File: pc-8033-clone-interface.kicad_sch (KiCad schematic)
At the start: 15 parts, among them J2 80s31, U2 74LS32, U3 74LS04, U4 82C55A, U5 74LS30

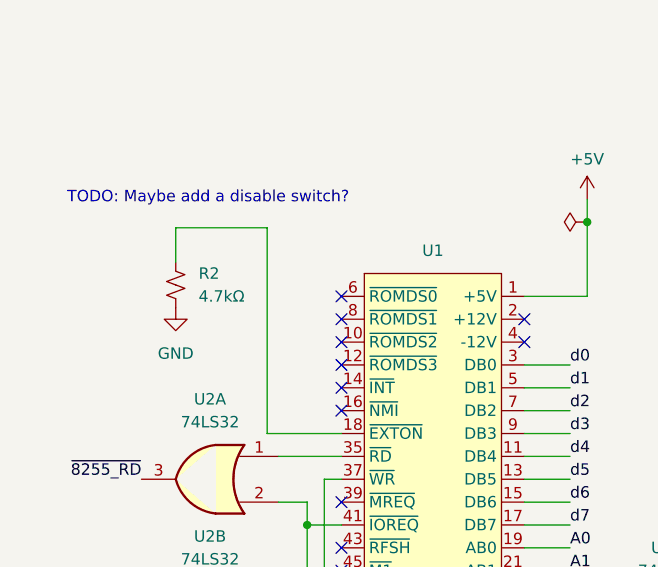
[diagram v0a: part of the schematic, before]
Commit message: Short the EXTON pin instead of trying to gently pull it down
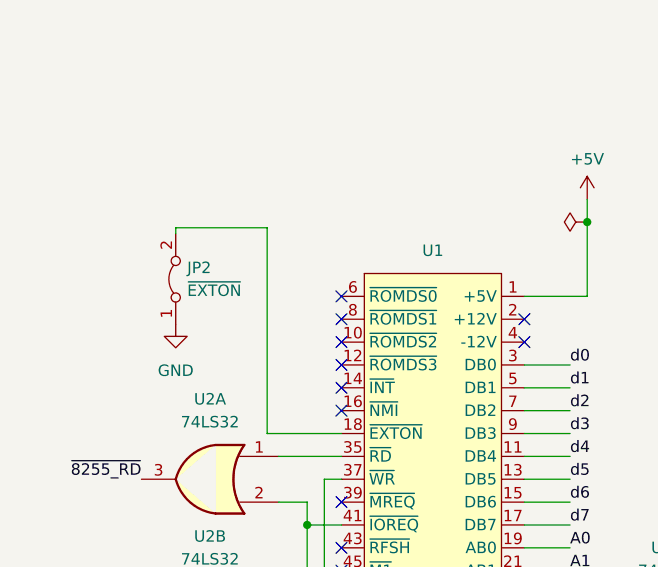
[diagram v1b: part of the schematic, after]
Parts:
- removed R2: 4.7kΩ, Resistor_THT:R_Axial_DIN0309_L9.0mm_D3.2mm_P12.70mm_Horizontal, symbol Device:R_Small_US
- added JP2: ~{EXTON}, Jumper:SolderJumper-2_P1.3mm_Bridged2Bar_Pad1.0x1.5mm, symbol Jumper:Jumper_2_Bridged
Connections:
- net GND: now also JP2.1 (A)
- net at U1.18 (~{EXTON}): now also JP2.2 (B)
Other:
- note removed: "TODO: Maybe add a disable switch?"
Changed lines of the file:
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@@
     (stroke (width 0) (type default))
   )
-  (wire (pts (xy 27.94 58.42) (xy 27.94 62.23))
+  (wire (pts (xy 27.94 58.42) (xy 27.94 59.055))
     (stroke (width 0) (type default))
   )
@@
   (text "This second inversion of reset appears to be important for timing purposes,\nas per https://blog.goo.ne.jp/tk-80/e/6ac4226f93ae2f80224ee7fcf31cb796"
     (at 166.37 158.75 0)
-    (effects (font (size 1.27 1.27)) (justify left bottom))
-  )
-  (text "TODO: Maybe add a disable switch?" (at 15.875 55.88 0)
     (effects (font (size 1.27 1.27)) (justify left bottom))
   )
@@
         (path "/9d504855-0dbe-4626-9ba5-7c5a4a75c091"
           (reference "#FLG02") (unit 1)
-        )
-      )
-    )
-  )
-  (symbol (lib_id "Device:R_Small_US") (at 27.94 64.77 0) (unit 1)
-    (in_bom yes) (on_board yes) (dnp no) (fields_autoplaced)
-    (property "Reference" "R2" (at 30.48 63.5 0)
-      (effects (font (size 1.27 1.27)) (justify left))
-    )
-    (property "Value" "4.7kΩ" (at 30.48 66.04 0)
-      (effects (font (size 1.27 1.27)) (justify left))
-    )
-    (property "Footprint" "Resistor_THT:R_Axial_DIN0309_L9.0mm_D3.2mm_P12.70mm_Horizontal" (at 27.94 64.77 0)
-      (effects (font (size 1.27 1.27)) hide)
-    )
-    (property "Datasheet" "~" (at 27.94 64.77 0)
-      (effects (font (size 1.27 1.27)) hide)
-    )
-    (pin "1")
-    (pin "2")
-    (instances
-      (project "pc-8033-clone-interface"
-        (path "/9d504855-0dbe-4626-9ba5-7c5a4a75c091"
-          (reference "R2") (unit 1)
         )
       )
@@
     )
   )
-  (symbol (lib_id "power:GND") (at 27.94 67.31 0) (unit 1)
-    (in_bom yes) (on_board yes) (dnp no) (fields_autoplaced)
-    (property "Reference" "#PWR016" (at 27.94 73.66 0)
-      (effects (font (size 1.27 1.27)) hide)
-    )
-    (property "Value" "GND" (at 27.94 72.39 0)
-      (effects (font (size 1.27 1.27)))
-    )
-    (property "Footprint" "" (at 27.94 67.31 0)
-      (effects (font (size 1.27 1.27)) hide)
-    )
-    (property "Datasheet" "" (at 27.94 67.31 0)
+  (symbol (lib_id "power:GND") (at 27.94 69.215 0) (unit 1)
+    (in_bom yes) (on_board yes) (dnp no) (fields_autoplaced)
+    (property "Reference" "#PWR016" (at 27.94 75.565 0)
+      (effects (font (size 1.27 1.27)) hide)
+    )
+    (property "Value" "GND" (at 27.94 74.295 0)
+      (effects (font (size 1.27 1.27)))
+    )
+    (property "Footprint" "" (at 27.94 69.215 0)
+      (effects (font (size 1.27 1.27)) hide)
+    )
+    (property "Datasheet" "" (at 27.94 69.215 0)
       (effects (font (size 1.27 1.27)) hide)
     )
@@
         )
       )
+    )
+  )
+  (symbol (lib_id "Jumper:Jumper_2_Bridged") (at 27.94 64.135 90) (unit 1)
+    (in_bom yes) (on_board yes) (dnp no) (fields_autoplaced)
+    (property "Reference" "JP2" (at 29.21 62.865 90)
+      (effects (font (size 1.27 1.27)) (justify right))
+    )
+    (property "Value" "~{EXTON}" (at 29.21 65.405 90)
+      (effects (font (size 1.27 1.27)) (justify right))
+    )
+    (property "Footprint" "Jumper:SolderJumper-2_P1.3mm_Bridged2Bar_Pad1.0x1.5mm" (at 27.94 64.135 0)
+      (effects (font (size 1.27 1.27)) hide)
+    )
+    (property "Datasheet" "~" (at 27.94 64.135 0)
+      (effects (font (size 1.27 1.27)) hide)
+    )
+    (pin "2")
+    (pin "1")
+    (instances
+      (project "pc-8033-clone-interface"
+        (path "/9d504855-0dbe-4626-9ba5-7c5a4a75c091"
+          (reference "JP2") (unit 1)
+        )
+      )

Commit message: add a smaller decoupling cap on the 8255
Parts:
- added C2: 0.1µF, Capacitor_THT:C_Disc_D3.4mm_W2.1mm_P2.50mm, symbol Device:C_Small
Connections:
- net +5V: now also C2.1
- net GND: now also C2.2
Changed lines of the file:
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@@
+    )
+  )
+  (symbol (lib_id "Device:C_Small") (at 102.235 127.635 0) (unit 1)
+    (in_bom yes) (on_board yes) (dnp no) (fields_autoplaced)
+    (property "Reference" "C2" (at 105.41 126.3713 0)
+      (effects (font (size 1.27 1.27)) (justify left))
+    )
+    (property "Value" "0.1µF" (at 105.41 128.9113 0)
+      (effects (font (size 1.27 1.27)) (justify left))
+    )
+    (property "Footprint" "Capacitor_THT:C_Disc_D3.4mm_W2.1mm_P2.50mm" (at 102.235 127.635 0)
+      (effects (font (size 1.27 1.27)) hide)
+    )
+    (property "Datasheet" "~" (at 102.235 127.635 0)
+      (effects (font (size 1.27 1.27)) hide)
+    )
+    (pin "1")
+    (pin "2")
+    (instances
+      (project "pc-8033-clone-interface"
+        (path "/9d504855-0dbe-4626-9ba5-7c5a4a75c091"
+          (reference "C2") (unit 1)
+        )
+      )
     )
   )
@@
         (path "/9d504855-0dbe-4626-9ba5-7c5a4a75c091"
           (reference "U5") (unit 1)
+        )
+      )
+    )
+  )
+  (symbol (lib_id "power:GND") (at 102.235 130.175 0) (unit 1)
+    (in_bom yes) (on_board yes) (dnp no) (fields_autoplaced)
+    (property "Reference" "#PWR023" (at 102.235 136.525 0)
+      (effects (font (size 1.27 1.27)) hide)
+    )
+    (property "Value" "GND" (at 102.235 134.62 0)
+      (effects (font (size 1.27 1.27)))
+    )
+    (property "Footprint" "" (at 102.235 130.175 0)
+      (effects (font (size 1.27 1.27)) hide)
+    )
+    (property "Datasheet" "" (at 102.235 130.175 0)
+      (effects (font (size 1.27 1.27)) hide)
+    )
+    (pin "1")
+    (instances
+      (project "pc-8033-clone-interface"
+        (path "/9d504855-0dbe-4626-9ba5-7c5a4a75c091"
+          (reference "#PWR023") (unit 1)
         )
       )
@@
         )
       )
+    )
+  )
+  (symbol (lib_id "power:+5V") (at 102.235 125.095 0) (unit 1)
+    (in_bom yes) (on_board yes) (dnp no) (fields_autoplaced)
+    (property "Reference" "#PWR022" (at 102.235 128.905 0)
+      (effects (font (size 1.27 1.27)) hide)
+    )
+    (property "Value" "+5V" (at 102.235 120.65 0)
+      (effects (font (size 1.27 1.27)))
+    )
+    (property "Footprint" "" (at 102.235 125.095 0)
+      (effects (font (size 1.27 1.27)) hide)
+    )
+    (property "Datasheet" "" (at 102.235 125.095 0)
+      (effects (font (size 1.27 1.27)) hide)
+    )
+    (pin "1")
+    (instances
+      (project "pc-8033-clone-interface"
+        (path "/9d504855-0dbe-4626-9ba5-7c5a4a75c091"
+          (reference "#PWR022") (unit 1)
+        )
+      )

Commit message: Use weird Centronics pinout on board
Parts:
- J2: footprint Connector_PinHeader_2.54mm:PinHeader_2x18_P2.54mm_Vertical -> PC-8001:Centronics_36_FDD
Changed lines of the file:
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@@
       (effects (font (size 1.27 1.27)))
     )
-    (property "Footprint" "Connector_PinHeader_2.54mm:PinHeader_2x18_P2.54mm_Vertical" (at 189.23 109.22 0)
+    (property "Footprint" "PC-8001:Centronics_36_FDD" (at 189.23 109.22 0)
       (effects (font (size 1.27 1.27)) hide)
     )

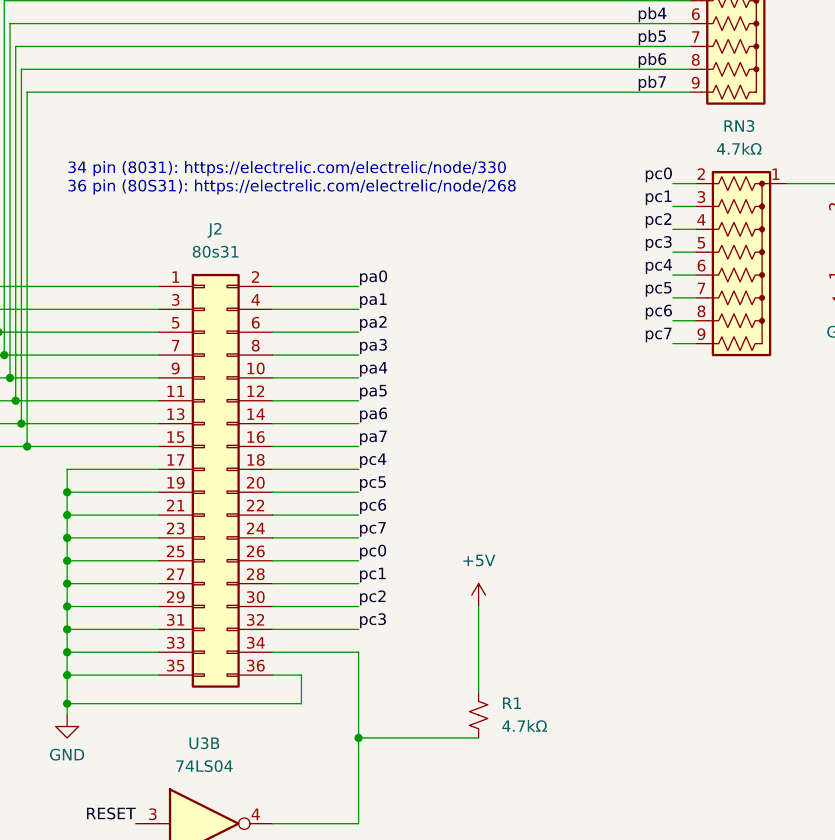
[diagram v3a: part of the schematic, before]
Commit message: V3: fix the pinout once and for all
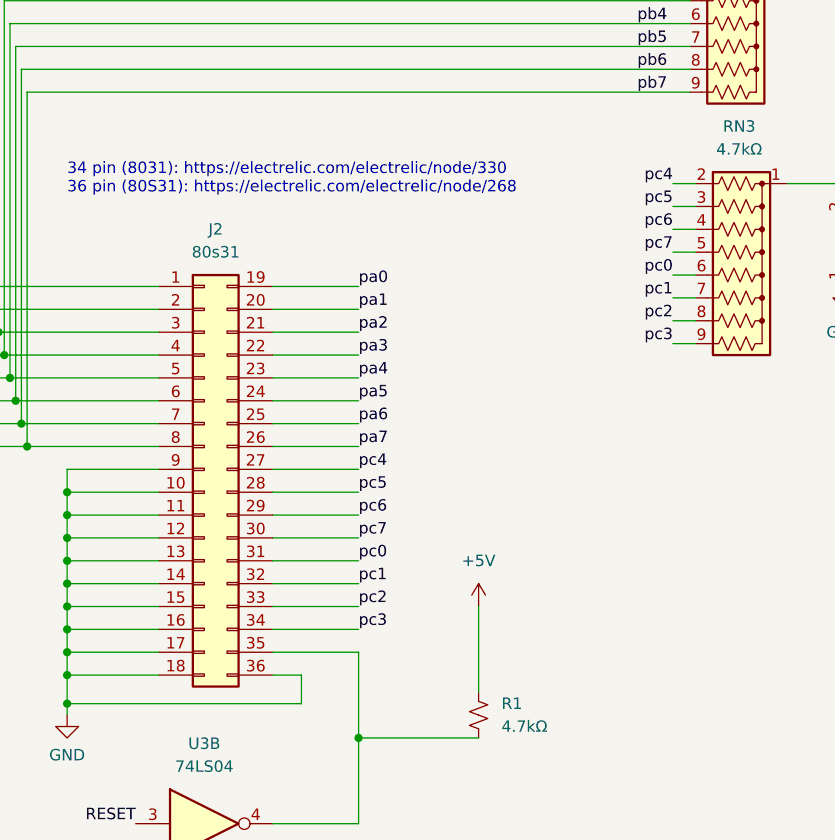
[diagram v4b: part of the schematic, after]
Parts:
- removed J2: 80s31, PC-8001:Centronics_36_FDD, symbol Connector_Generic:Conn_02x18_Odd_Even
- added J2: 80s31, PC-8001:Centronics_36_FDD, symbol Connector_Generic:Conn_02x18_Top_Bottom
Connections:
- net GND: now also J2.10 (Pin_10), J2.11 (Pin_11), J2.12 (Pin_12), J2.13 (Pin_13), J2.14 (Pin_14), J2.15 (Pin_15), J2.16 (Pin_16), J2.17 (Pin_17), J2.18 (Pin_18), J2.36 (Pin_36), J2.9 (Pin_9)
- net pa0: now also J2.19 (Pin_19)
- net pa1: now also J2.20 (Pin_20)
- net pa2: now also J2.21 (Pin_21)
- net pa3: now also J2.22 (Pin_22)
- net pa4: now also J2.23 (Pin_23)
- net pa5: now also J2.24 (Pin_24)
- net pa6: now also J2.25 (Pin_25)
- net pa7: now also J2.26 (Pin_26)
- net pb0: now also J2.1 (Pin_1)
- net pb1: now also J2.2 (Pin_2)
- net pb2: now also J2.3 (Pin_3)
- net pb3: now also J2.4 (Pin_4)
- net pb4: now also J2.5 (Pin_5)
- net pb5: now also J2.6 (Pin_6)
- net pb6: now also J2.7 (Pin_7)
- net pb7: now also J2.8 (Pin_8)
- net pc0: now also RN3.6 (R5), J2.31 (Pin_31); no longer RN3.2 (R1)
- net pc1: now also RN3.7 (R6), J2.32 (Pin_32); no longer RN3.3 (R2)
- net pc2: now also RN3.8 (R7), J2.33 (Pin_33); no longer RN3.4 (R3)
- net pc3: now also RN3.9 (R8), J2.34 (Pin_34); no longer RN3.5 (R4)
- net pc4: now also RN3.2 (R1), J2.27 (Pin_27); no longer RN3.6 (R5)
- net pc5: now also RN3.3 (R2), J2.28 (Pin_28); no longer RN3.7 (R6)
- net pc6: now also RN3.4 (R3), J2.29 (Pin_29); no longer RN3.8 (R7)
- net pc7: now also RN3.5 (R4), J2.30 (Pin_30); no longer RN3.9 (R8)
- net at R1.2, U3.4: now also J2.35 (Pin_35)

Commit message: Fix select logic
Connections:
- net +5V: now also U5.11, U5.12
- net GND: no longer U5.11, U5.12
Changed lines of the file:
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@@
   (junction (at 167.64 99.06) (diameter 0) (color 0 0 0 0)
   )
+  (junction (at 72.39 116.84) (diameter 0) (color 0 0 0 0)
+  )
   (junction (at 113.03 160.655) (diameter 0) (color 0 0 0 0)
   )
@@
   )
   (junction (at 169.545 106.68) (diameter 0) (color 0 0 0 0)
-  )
-  (junction (at 74.93 116.84) (diameter 0) (color 0 0 0 0)
   )
   (junction (at 173.99 116.84) (diameter 0) (color 0 0 0 0)
@@
     (stroke (width 0) (type default))
   )
+  (wire (pts (xy 72.39 116.84) (xy 74.93 116.84))
+    (stroke (width 0) (type default))
+  )
   (wire (pts (xy 173.99 114.3) (xy 173.99 111.76))
     (stroke (width 0) (type default))
@@
     (stroke (width 0) (type default))
   )
+  (wire (pts (xy 72.39 114.3) (xy 74.93 114.3))
+    (stroke (width 0) (type default))
+  )
   (wire (pts (xy 241.3 92.71) (xy 243.84 92.71))
     (stroke (width 0) (type default))
@@
     (stroke (width 0) (type default))
   )
+  (wire (pts (xy 72.39 125.73) (xy 72.39 116.84))
+    (stroke (width 0) (type default))
+  )
   (wire (pts (xy 173.99 124.46) (xy 173.99 121.92))
     (stroke (width 0) (type default))
@@
     (stroke (width 0) (type default))
   )
+  (wire (pts (xy 87.63 120.65) (xy 87.63 125.73))
+    (stroke (width 0) (type default))
+  )
   (wire (pts (xy 66.675 76.2) (xy 71.755 76.2))
     (stroke (width 0) (type default))
@@
     (stroke (width 0) (type default))
   )
+  (wire (pts (xy 72.39 116.84) (xy 72.39 114.3))
+    (stroke (width 0) (type default))
+  )
   (wire (pts (xy 168.91 64.77) (xy 168.91 104.14))
     (stroke (width 0) (type default))
@@
     (stroke (width 0) (type default))
   )
+  (wire (pts (xy 87.63 125.73) (xy 72.39 125.73))
+    (stroke (width 0) (type default))
+  )
   (wire (pts (xy 168.91 104.14) (xy 184.15 104.14))
     (stroke (width 0) (type default))
@@
     (stroke (width 0) (type default))
   )
-  (wire (pts (xy 74.93 114.3) (xy 74.93 116.84))
-    (stroke (width 0) (type default))
-  )
   (wire (pts (xy 173.99 114.3) (xy 184.15 114.3))
     (stroke (width 0) (type default))
@@
   )
   (wire (pts (xy 113.03 160.655) (xy 113.03 147.32))
-    (stroke (width 0) (type default))
-  )
-  (wire (pts (xy 74.93 116.84) (xy 74.93 120.65))
     (stroke (width 0) (type default))
   )
@@
         (path "/9d504855-0dbe-4626-9ba5-7c5a4a75c091"
           (reference "#FLG02") (unit 1)
+        )
+      )
+    )
+  )
+  (symbol (lib_id "power:+5V") (at 87.63 120.65 0) (unit 1)
+    (in_bom yes) (on_board yes) (dnp no) (fields_autoplaced)
+    (property "Reference" "#PWR05" (at 87.63 124.46 0)
+      (effects (font (size 1.27 1.27)) hide)
+    )
+    (property "Value" "+5V" (at 87.63 115.57 0)
+      (effects (font (size 1.27 1.27)))
+    )
+    (property "Footprint" "" (at 87.63 120.65 0)
+      (effects (font (size 1.27 1.27)) hide)
+    )
+    (property "Datasheet" "" (at 87.63 120.65 0)
+      (effects (font (size 1.27 1.27)) hide)
+    )
+    (pin "1")
+    (instances
+      (project "pc-8033-clone-interface"
+        (path "/9d504855-0dbe-4626-9ba5-7c5a4a75c091"
+          (reference "#PWR05") (unit 1)
         )
       )
@@
         )
       )
-    )
-  )
-  (symbol (lib_id "power:GND") (at 74.93 120.65 0) (unit 1)
-    (in_bom yes) (on_board yes) (dnp no) (fields_autoplaced)
-    (property "Reference" "#PWR05" (at 74.93 127 0)
-      (effects (font (size 1.27 1.27)) hide)
-    )
-    (property "Value" "GND" (at 74.93 125.73 0)
-      (effects (font (size 1.27 1.27)))
-    )
-    (property "Footprint" "" (at 74.93 120.65 0)
-      (effects (font (size 1.27 1.27)) hide)
-    )
-    (property "Datasheet" "" (at 74.93 120.65 0)
-      (effects (font (size 1.27 1.27)) hide)
-    )
-    (pin "1")
-    (instances
-      (project "pc-8033-clone-interface"
-        (path "/9d504855-0dbe-4626-9ba5-7c5a4a75c091"
-          (reference "#PWR05") (unit 1)
-        )
-      )
